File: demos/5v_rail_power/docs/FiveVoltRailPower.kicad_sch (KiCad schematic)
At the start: 7 parts, among them P1 Header1xNMale, U1 L7805

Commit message: export: kicad_sch — Phase 2.5b: layered placement, wire routing, KiCad 10 compatibility (#23)
* export: kicad_sch — Phase 2.5b: layered placement + routing + KiCad 9 fix

Placement (placement.py, complete rewrite):
- Replaces naive grid with Layered Signal Flow algorithm (spec §5 stages 1–8)
- Stage 1: band classification — power chips/rails at top, LEDs at bottom,
  everything else in the signal band
- Stage 2: signal-flow DAG via BFS from Rail/Connector sources; layer = BFS
  distance from nearest source
- Stage 3–4: place within (band, layer) cells at 1500-mil (38.1 mm) same-band
  spacing, 1000-mil inter-band gutter, 25.4 mm page margin
- Stage 6: cluster breakup — up to 10 iterations shifting same-band parts
  that land closer than 0.9× SAME_BAND_SPACING_MM
- Stage 8: page sized to fit (A4 → A3 → A2 → A1)
- grid_place() and sheet_size_mm() kept as shims for backward-compat

Routing (routing.py, new file):
- route_net(): connects stub ends with Manhattan L-shapes (horizontal first)
- find_junctions(): returns points where ≥3 wire endpoints coincide
- renderer uses routed wires between signal-net stub ends

Hierarchical (hierarchical.py, new file):
- collect_boards(), is_multi_board(), sub_sheet_filename() — interface stub
  for multi-Board sub-sheet emission (full implementation deferred)

KiCad 9 sub-symbol name fix (library_loader.py):
- KiCad 9 schematics expect sub-symbols nested inside their parent in
  lib_symbols to use the bare name (R_0_1, LED_0_1, 4069_1_0) — NOT the
  lib-qualified name (Device:R_0_1, Device:LED_0_1, 4xxx:4069_1_0)
- Fixed _qualify_names() to add the lib: prefix only to the exact parent
  symbol name using a lookahead (?=") that prevents sub-unit names from
  being qualified

Tests (+25 tests):
- test_placement.py: band classification, all-on-grid, determinism,
  minimum spacing, power < signal < indicator Y ordering, page sizing
- test_routing.py: H/V segments, L-shapes, orthogonality, grid snap,
  junction detection

Golden files re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
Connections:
- net Net-(C1-t1) is gone; now on net Net-(BT1-neg): C1.2, U1.1 (IN)
- net Net-(D3-anode) is gone; now on net Net-(C2-t1): D3.1 (K), R1.1
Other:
- moved on the sheet: C1, C2, D1, D3, P1, R1, U1

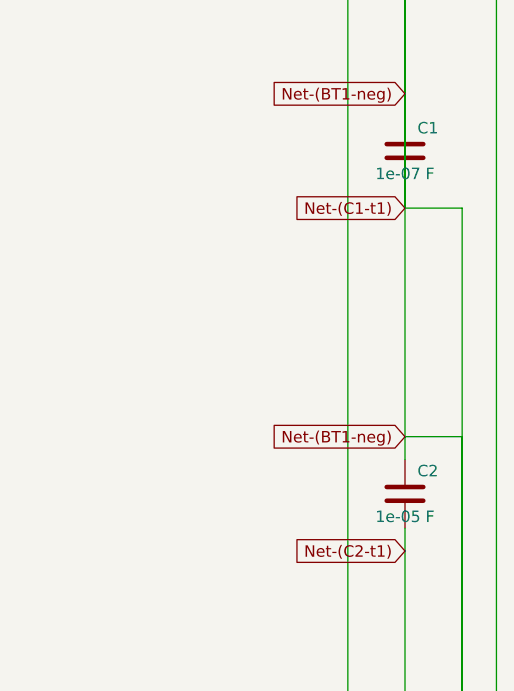
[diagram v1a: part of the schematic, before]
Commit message: units: Ohms.__str__ uses engineering notation (kΩ, MΩ, GΩ) (#33)
* units: Ohms.__str__ uses engineering notation (kΩ, MΩ, GΩ)

The previous `Ohms.__str__` formatted with bare `:.3g`, producing
unreadable scientific output for clean kilo / mega multiples:

  str(Ohms(10_000))     == "1e+04 Ω"      → now "10 kΩ"
  str(Ohms(100_000))    == "1e+05 Ω"      → now "100 kΩ"
  str(Ohms(1_000_000))  == "1e+06 Ω"      → now "1 MΩ"

The breadboard SVG visualiser surfaced the problem: a resistor body
labelled "100000Ω" makes a reader count zeros, while a label of
"100 kΩ" reads at a glance — exactly the convention every schematic
and parts catalogue uses. Centralising the engineering notation in
`Ohms.__str__` means every downstream consumer (assembly guide,
breadboard SVG, kicad netlist, BOM, reports) inherits the readable
form without each format adapter rolling its own formatter.

  - `Ohms.__str__` returns "47 Ω", "4.7 kΩ", "10 kΩ", "100 kΩ",
    "1 MΩ", "10 MΩ", "1 GΩ" per the kilo / mega / giga thresholds.
  - `Resistor.__str__` delegates to `str(self._ohms)` so it
    inherits the new notation (was producing the noisy "47.0 Ω"
    via raw float).
  - The breadboard visualiser's resistor body label uses
    `str(part.ohms)` directly (previously had a private
    `_format_ohms_compact` helper; removed).
  - `tests/components/test_resistor.py::test_str` updated for
    "47 Ω" (was "47.0 Ω"); new `test_str_renders_in_engineering_notation`
    pins kΩ / MΩ output across the kilo and mega thresholds.
  - All demo docs / goldens refreshed where the Ohms.__str__
    change affected the rendered output (breadboard SVGs, kicad
    sch value fields, BOM rows).

* units: Farads + Henries __str__ also use engineering notation

Same treatment as `Ohms.__str__` (previous commit) for the other two
passive engineering quantities. Demos contain caps and inductors
with values that the bare `:.3g` formatter would emit in scientific
form (`1e-07 F` for a 100 nF decoupling cap); centralising t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
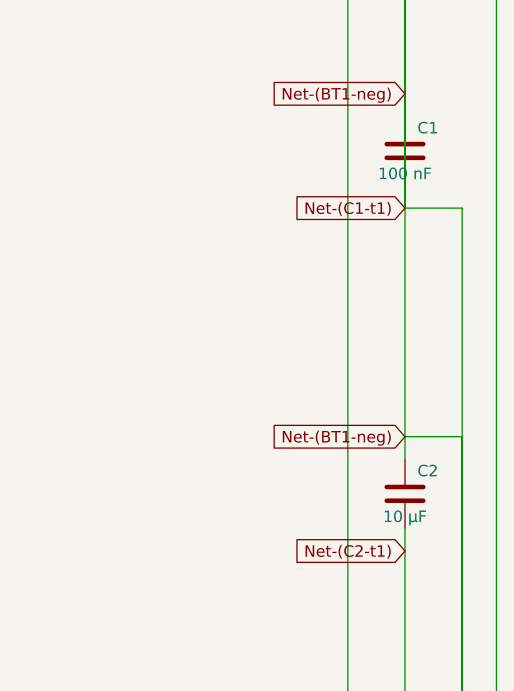
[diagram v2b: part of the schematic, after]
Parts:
- C1: value 1e-07 F -> 100 nF
- C2: value 1e-05 F -> 10 µF
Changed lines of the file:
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@@
       (effects (font (size 1.27 1.27)))
     )
-    (property "Value" "1e-07 F"
+    (property "Value" "100 nF"
       (at 63.5 129.54 0)
       (effects (font (size 1.27 1.27)))
@@
       (effects (font (size 1.27 1.27)))
     )
-    (property "Value" "1e-05 F"
+    (property "Value" "10 µF"
       (at 63.5 167.64 0)
       (effects (font (size 1.27 1.27)))
